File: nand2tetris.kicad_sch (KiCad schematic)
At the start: 28 parts

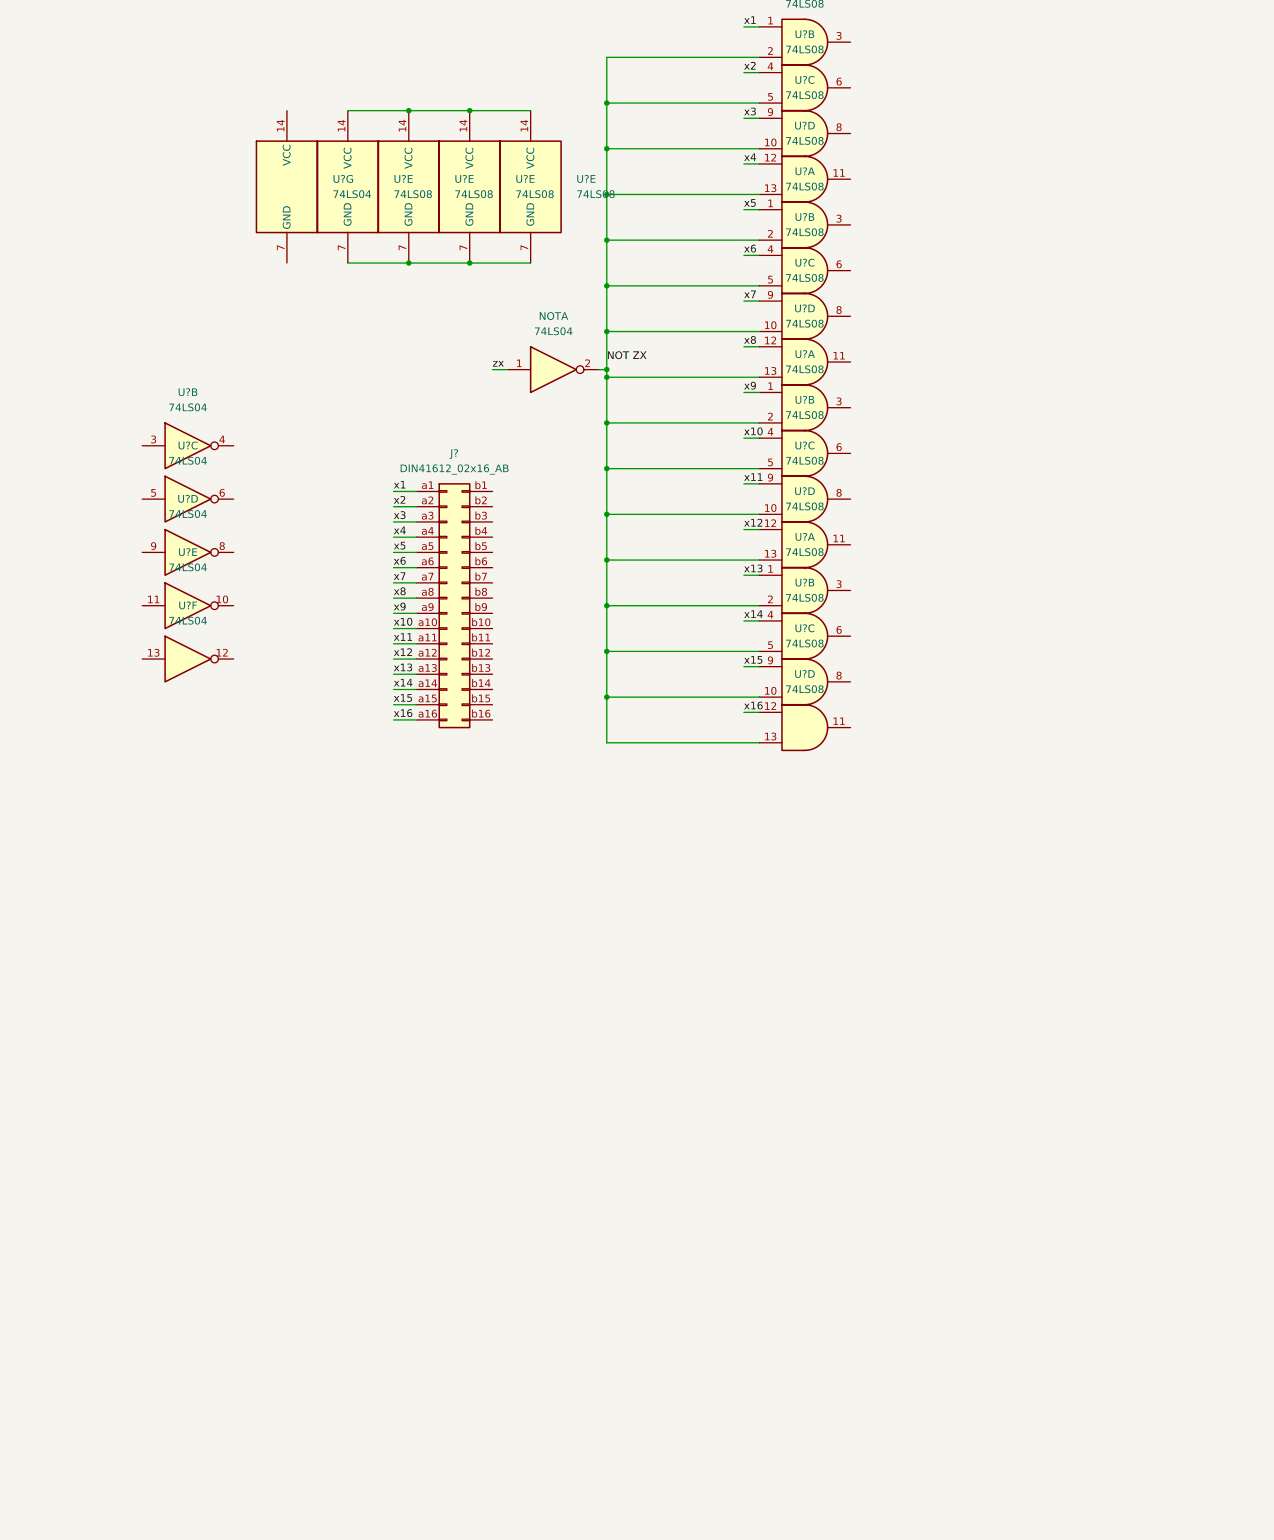
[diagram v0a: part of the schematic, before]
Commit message: Add xor module and sub-page
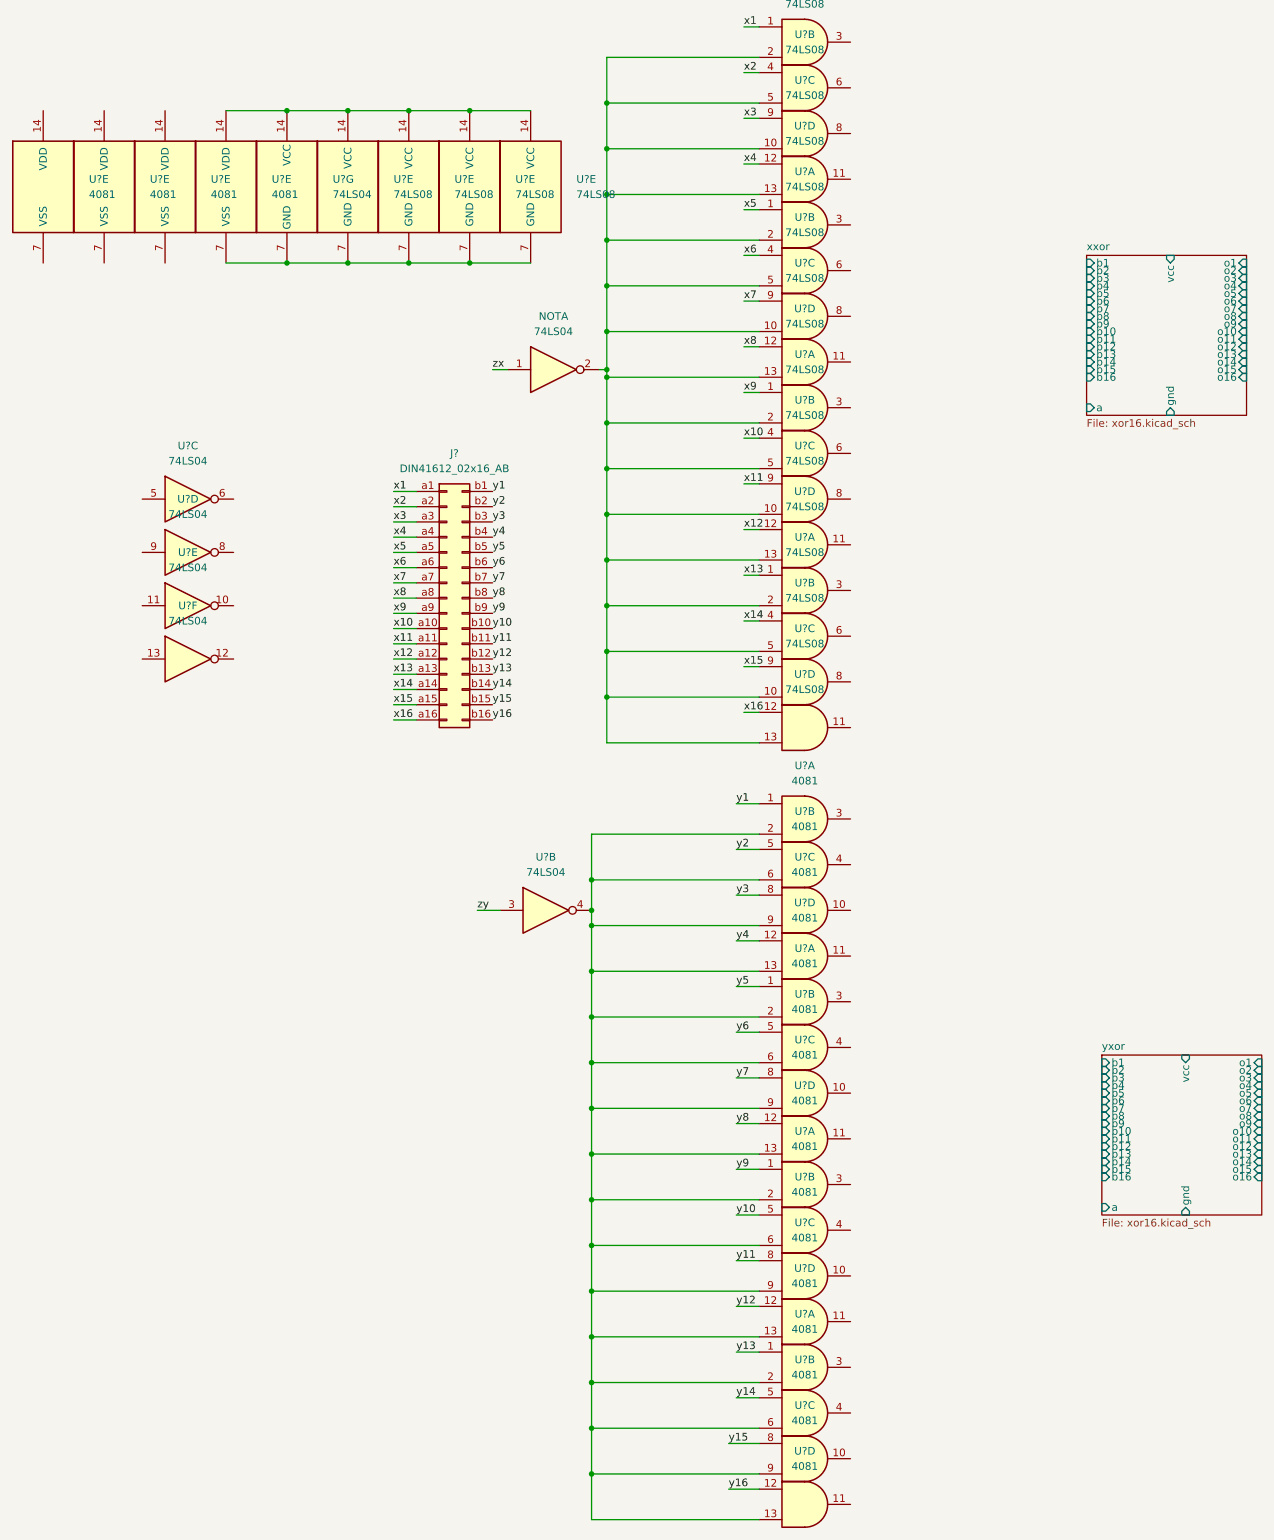
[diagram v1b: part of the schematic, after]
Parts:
- added U? (x20): 4081, symbol 4xxx:4081
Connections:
- net y1: now reaches J?.b1 (Pin_b1)
- net y1: now also U?.1
- net y10: now reaches J?.b10 (Pin_b10)
- net y10: now also U?.5
- net y11: now reaches J?.b11 (Pin_b11)
- net y11: now also U?.8
- net y12: now reaches J?.b12 (Pin_b12)
- net y12: now also U?.12
- net y13: now reaches J?.b13 (Pin_b13)
- net y13: now also U?.1
- net y14: now reaches J?.b14 (Pin_b14)
- net y14: now also U?.5
- net y15: now reaches J?.b15 (Pin_b15)
- net y15: now also U?.8
- net y16: now reaches J?.b16 (Pin_b16)
- net y16: now also U?.12
- net y2: now reaches J?.b2 (Pin_b2)
- net y2: now also U?.5
- net y3: now reaches J?.b3 (Pin_b3)
- net y3: now also U?.8
- net y4: now reaches J?.b4 (Pin_b4)
- net y4: now also U?.12
- net y5: now reaches J?.b5 (Pin_b5)
- net y5: now also U?.1
- net y6: now reaches J?.b6 (Pin_b6)
- net y6: now also U?.5
- net y7: now reaches J?.b7 (Pin_b7)
- net y7: now also U?.8
- net y8: now reaches J?.b8 (Pin_b8)
- net y8: now also U?.12
- net y9: now reaches J?.b9 (Pin_b9)
- net y9: now also U?.1
- net zy: now reaches U?.3
- net at U?.4: now also U?.13, U?.13, U?.13, U?.13, U?.2, U?.2, U?.2, U?.2, U?.6, U?.6, U?.6, U?.6, U?.9, U?.9, U?.9, U?.9
- net at U?.14 (VCC): now also U?.14 (VCC), U?.14 (VCC), U?.14 (VCC), U?.14 (VCC), U?.14 (VDD)
- net at U?.7 (GND): now also U?.7 (GND), U?.7 (GND), U?.7 (GND), U?.7 (GND), U?.7 (VSS)
- net NOT ZX: no longer names the net of NOT.2, U?.10, U?.10, U?.10, U?.10, U?.13, U?.13, U?.13, U?.13, U?.2, U?.2, U?.2, U?.2, U?.5, U?.5, U?.5, U?.5
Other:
- added sheet xxor (xor16.kicad_sch)
- added sheet yxor (xor16.kicad_sch)
- moved on the sheet: U?B

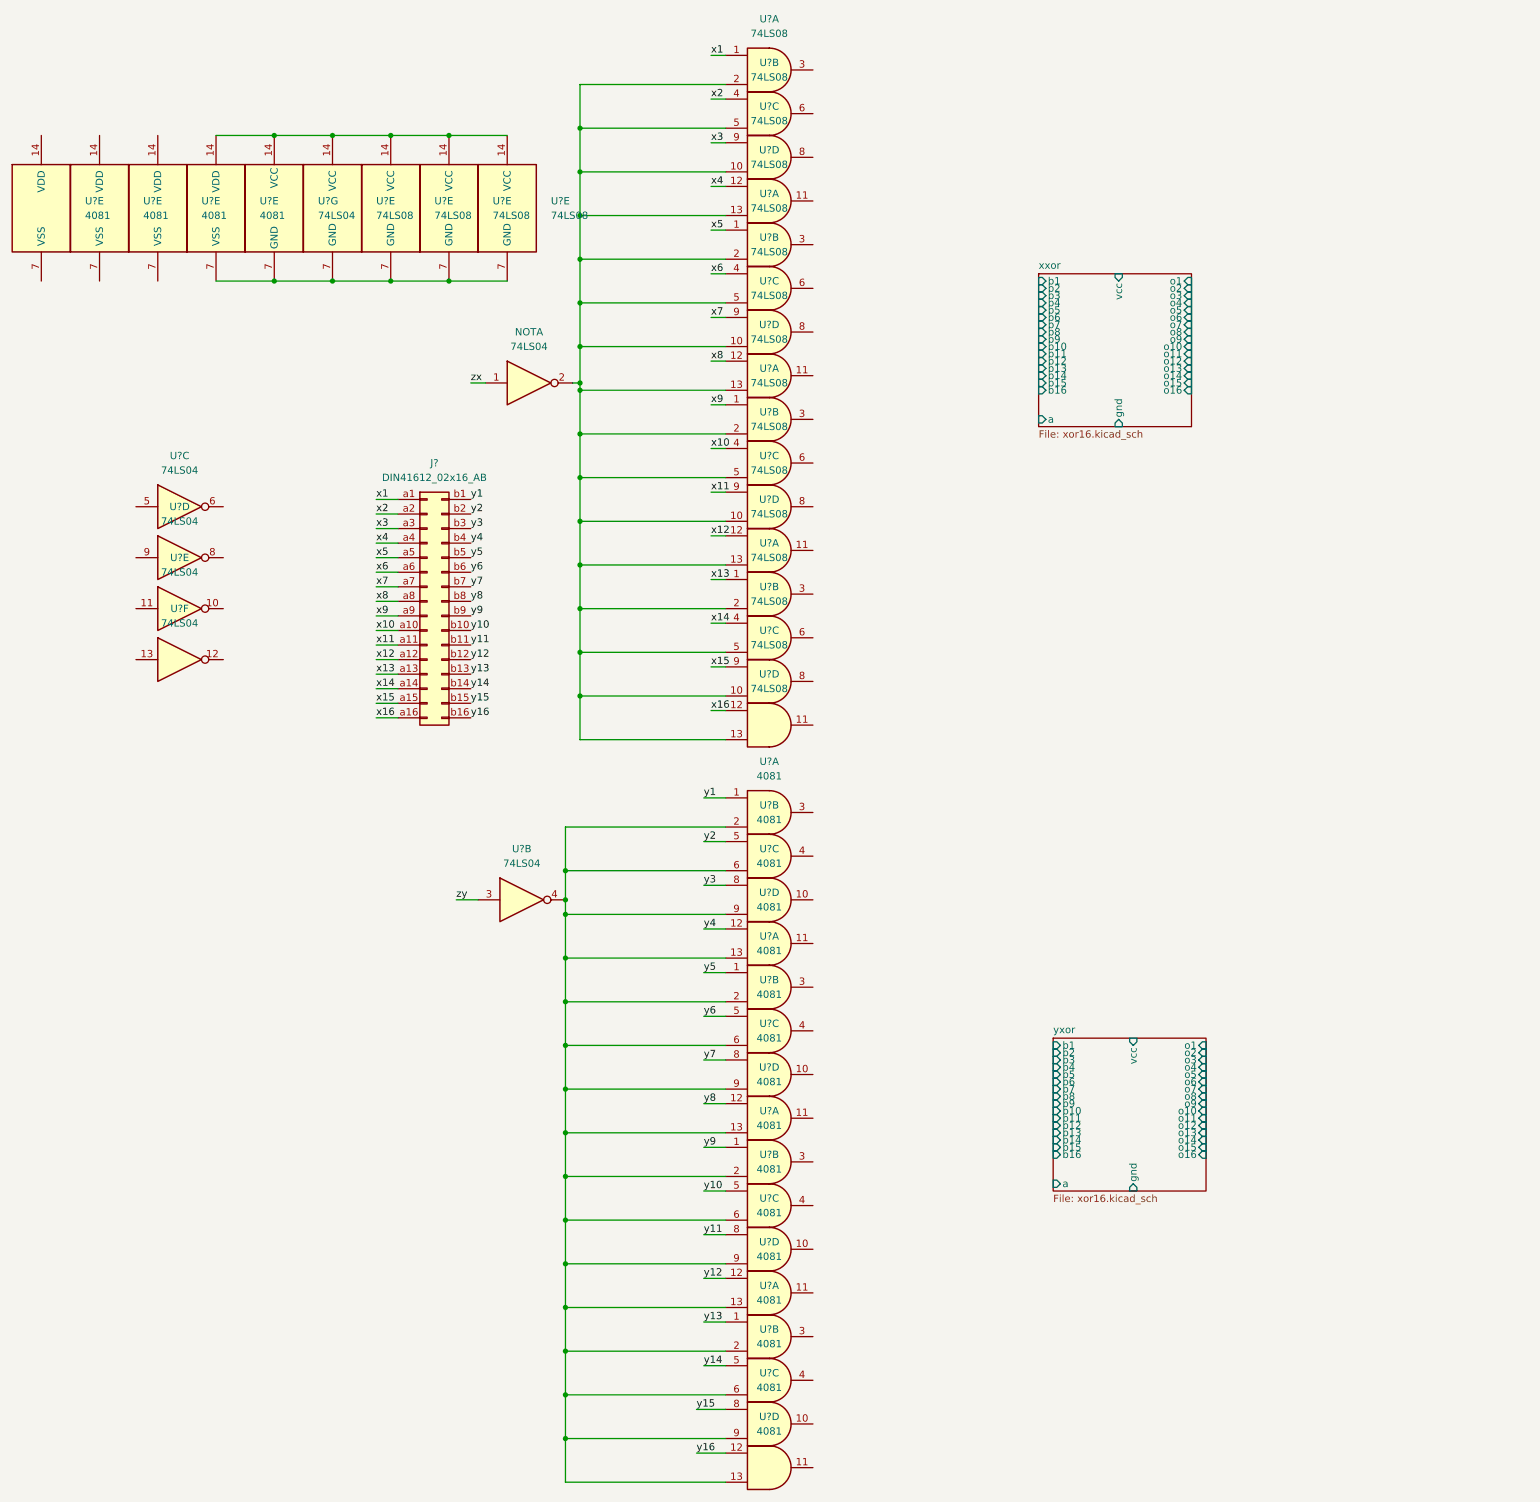
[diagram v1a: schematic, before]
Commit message: Add and16 and cleanup schematic
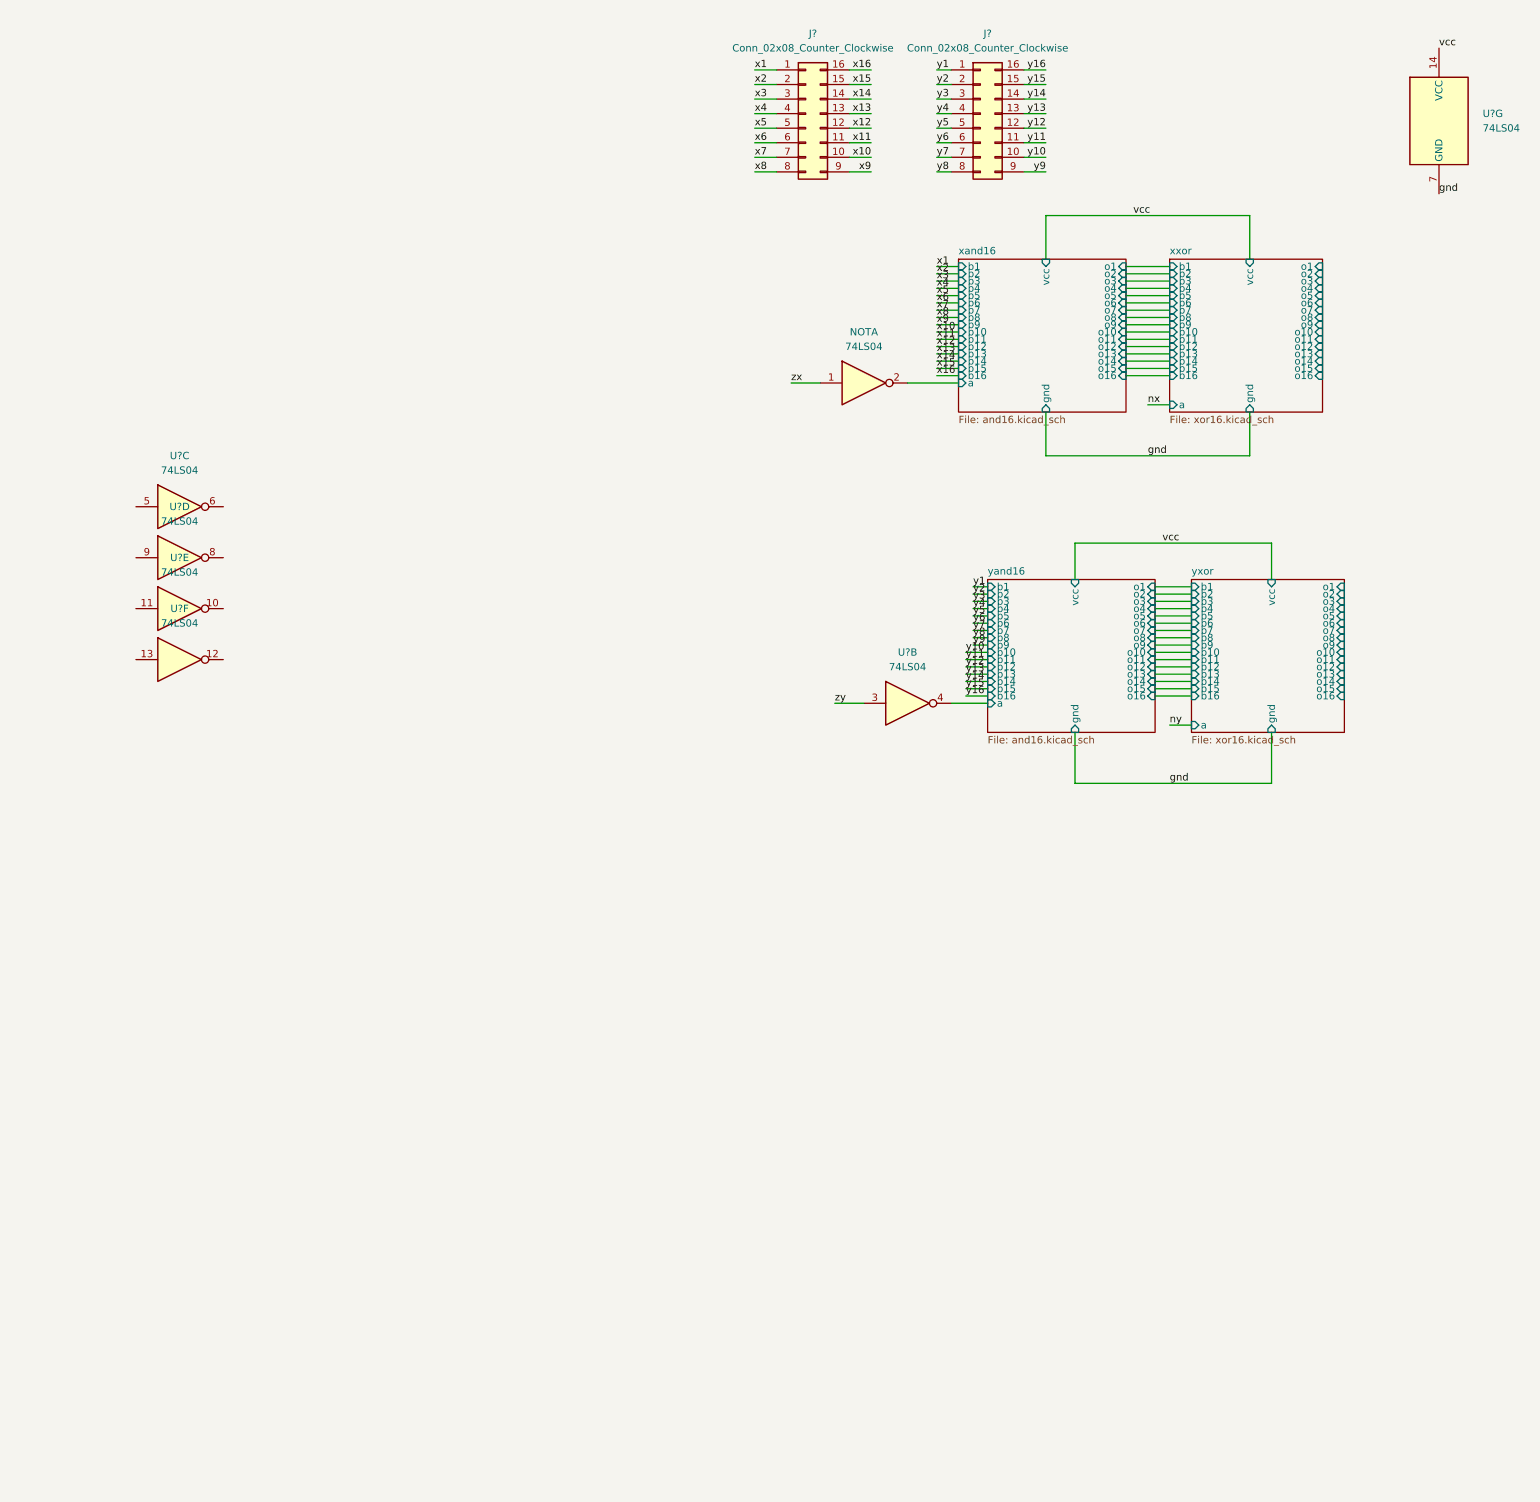
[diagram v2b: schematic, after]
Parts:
- removed J?: DIN41612_02x16_AB, symbol Connector:DIN41612_02x16_AB
- removed U? (x20): 4081, symbol 4xxx:4081
- removed U? (x20): 74LS08, symbol 74xx:74LS08
- added J? (x2): Conn_02x08_Counter_Clockwise, symbol Connector_Generic:Conn_02x08_Counter_Clockwise
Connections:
- net x1: now also J?.1 (Pin_1)
- net x10: now also J?.10 (Pin_10)
- net x11: now also J?.11 (Pin_11)
- net x12: now also J?.12 (Pin_12)
- net x13: now also J?.13 (Pin_13)
- net x14: now also J?.14 (Pin_14)
- net x15: now also J?.15 (Pin_15)
- net x16: now also J?.16 (Pin_16)
- net x2: now also J?.2 (Pin_2)
- net x3: now also J?.3 (Pin_3)
- net x4: now also J?.4 (Pin_4)
- net x5: now also J?.5 (Pin_5)
- net x6: now also J?.6 (Pin_6)
- net x7: now also J?.7 (Pin_7)
- net x8: now also J?.8 (Pin_8)
- net x9: now also J?.9 (Pin_9)
- net y1: now also J?.1 (Pin_1)
- net y10: now also J?.10 (Pin_10)
- net y11: now also J?.11 (Pin_11)
- net y12: now also J?.12 (Pin_12)
- net y13: now also J?.13 (Pin_13)
- net y14: now also J?.14 (Pin_14)
- net y15: now also J?.15 (Pin_15)
- net y16: now also J?.16 (Pin_16)
- net y2: now also J?.2 (Pin_2)
- net y3: now also J?.3 (Pin_3)
- net y4: now also J?.4 (Pin_4)
- net y5: now also J?.5 (Pin_5)
- net y6: now also J?.6 (Pin_6)
- net y7: now also J?.7 (Pin_7)
- net y8: now also J?.8 (Pin_8)
- net y9: now also J?.9 (Pin_9)
- net yand16/a: now reaches U?.4
- net xand16/a: now reaches NOT.2
- net vcc: now reaches U?.14 (VCC)
- net gnd: now reaches U?.7 (GND)
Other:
- added sheet xand16 (and16.kicad_sch)
- added sheet yand16 (and16.kicad_sch)
- moved on the sheet: NOTA, U?B, U?G
